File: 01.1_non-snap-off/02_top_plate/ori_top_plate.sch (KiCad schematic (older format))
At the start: 71 parts, among them U1 HOLE, U10 HOLE, U11 HOLE, U12 HOLE, U13 HOLE, U14 HOLE, U15 HOLE, U16 HOLE, U17 HOLE, U18 HOLE, U19 HOLE, U2 HOLE, U20 HOLE, U21 HOLE, U22 HOLE, U23 HOLE, U24 HOLE, U25 HOLE, U26 HOLE, U27 HOLE, U28 HOLE, U29 HOLE, U3 HOLE, U30 HOLE, U31 HOLE, U32 HOLE, U33 HOLE, U34 HOLE, U35 HOLE, U36 HOLE, U37 HOLE, U38 HOLE, U39 HOLE, U4 HOLE, U40 HOLE, U41 HOLE, U42 HOLE, U43 HOLE, U44 HOLE, U45 HOLE, U46 HOLE, U47 HOLE, U48 HOLE, U49 HOLE, U5 HOLE, U50 HOLE, U51 HOLE, U52 HOLE, U6 HOLE, U7 HOLE, U8 HOLE, U9 HOLE

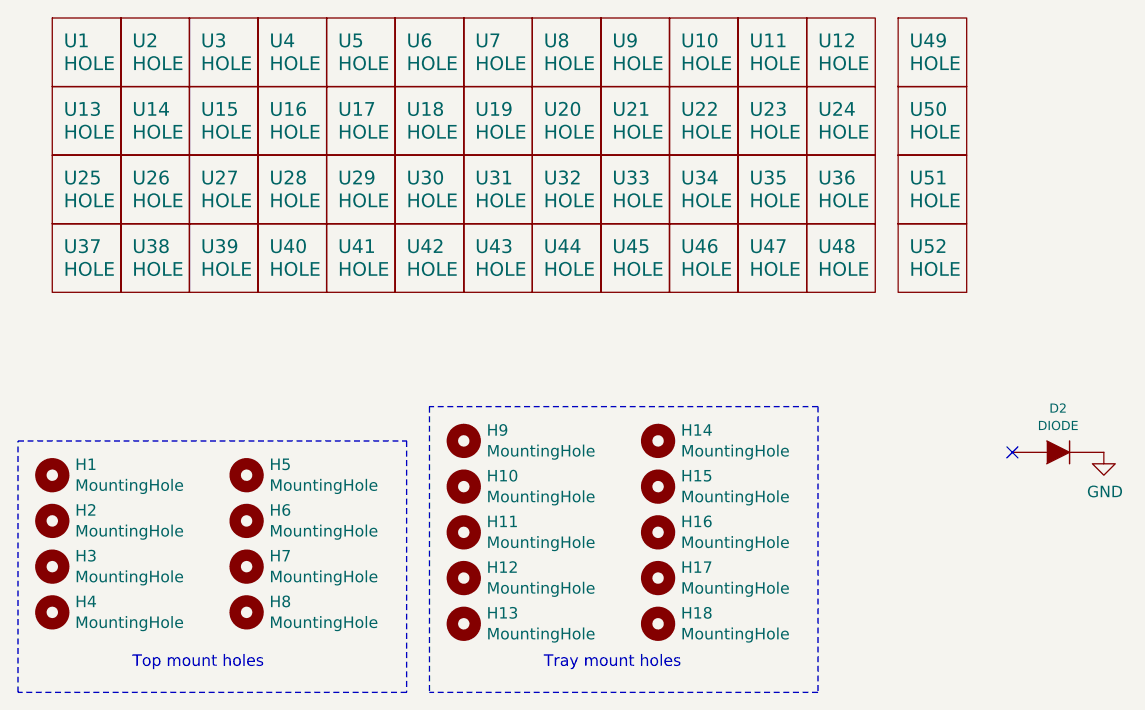
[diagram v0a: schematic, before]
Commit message: moved mounting holes
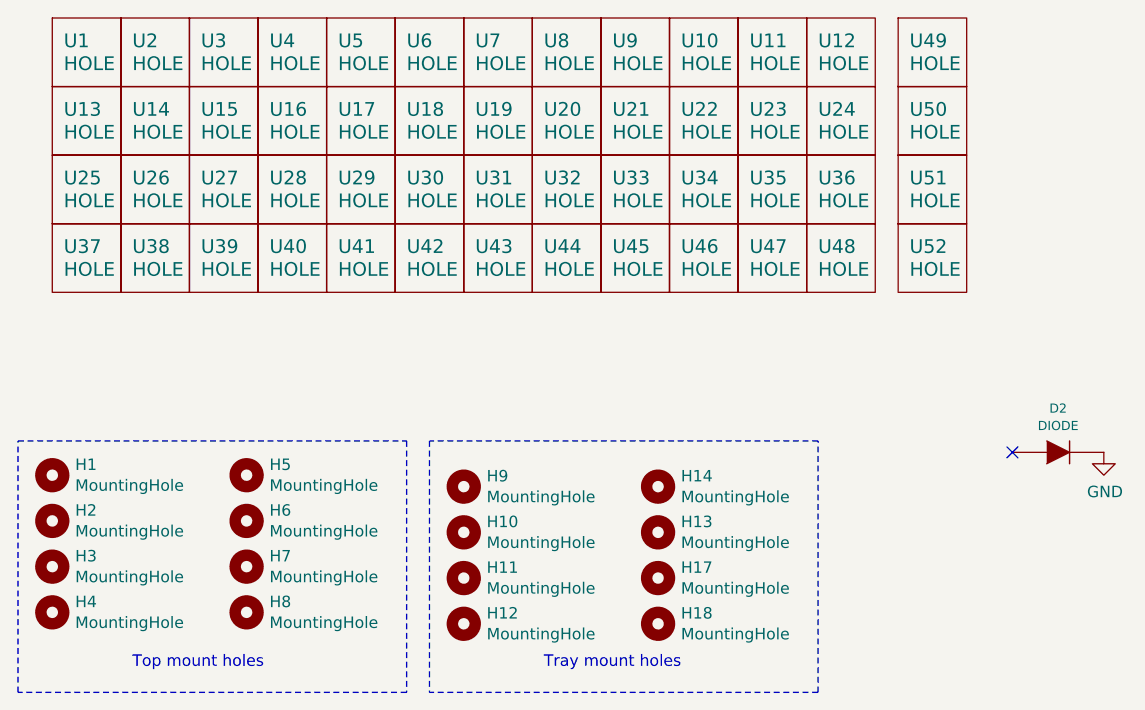
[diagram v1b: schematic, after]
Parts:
- removed H15, H16: MountingHole, MountingHole:MountingHole_2.2mm_M2_DIN965, symbol Mechanical:MountingHole
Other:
- moved on the sheet: H10, H11, H12, H13, H14, H9
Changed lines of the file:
@@
 L Mechanical:MountingHole H9
 U 1 1 6122943F
-P 4300 3250
-F 0 "H9" H 4400 3296 50  0000 L CNN
-F 1 "MountingHole" H 4400 3205 50  0000 L CNN
-F 2 "MountingHole:MountingHole_2.2mm_M2_DIN965" H 4300 3250 50  0001 C CNN
-F 3 "~" H 4300 3250 50  0001 C CNN
-	1    4300 3250
-	1    0    0    -1
-$EndComp
-$Comp
-L Mechanical:MountingHole H10
-U 1 1 61229445
 P 4300 3450
-F 0 "H10" H 4400 3496 50  0000 L CNN
+F 0 "H9" H 4400 3496 50  0000 L CNN
 F 1 "MountingHole" H 4400 3405 50  0000 L CNN
 F 2 "MountingHole:MountingHole_2.2mm_M2_DIN965" H 4300 3450 50  0001 C CNN
@@
 $EndComp
 $Comp
-L Mechanical:MountingHole H11
-U 1 1 6122944B
+L Mechanical:MountingHole H10
+U 1 1 61229445
 P 4300 3650
-F 0 "H11" H 4400 3696 50  0000 L CNN
+F 0 "H10" H 4400 3696 50  0000 L CNN
 F 1 "MountingHole" H 4400 3605 50  0000 L CNN
 F 2 "MountingHole:MountingHole_2.2mm_M2_DIN965" H 4300 3650 50  0001 C CNN
@@
 $EndComp
 $Comp
-L Mechanical:MountingHole H12
-U 1 1 61229451
+L Mechanical:MountingHole H11
+U 1 1 6122944B
 P 4300 3850
-F 0 "H12" H 4400 3896 50  0000 L CNN
+F 0 "H11" H 4400 3896 50  0000 L CNN
 F 1 "MountingHole" H 4400 3805 50  0000 L CNN
 F 2 "MountingHole:MountingHole_2.2mm_M2_DIN965" H 4300 3850 50  0001 C CNN
@@
 $EndComp
 $Comp
-L Mechanical:MountingHole H13
-U 1 1 61229457
+L Mechanical:MountingHole H12
+U 1 1 61229451
 P 4300 4050
-F 0 "H13" H 4400 4096 50  0000 L CNN
+F 0 "H12" H 4400 4096 50  0000 L CNN
 F 1 "MountingHole" H 4400 4005 50  0000 L CNN
 F 2 "MountingHole:MountingHole_2.2mm_M2_DIN965" H 4300 4050 50  0001 C CNN
@@
 $EndComp
 $Comp
-L Mechanical:MountingHole H14
-U 1 1 6122945D
-P 5150 3250
-F 0 "H14" H 5250 3296 50  0000 L CNN
-F 1 "MountingHole" H 5250 3205 50  0000 L CNN
-F 2 "MountingHole:MountingHole_2.2mm_M2_DIN965" H 5150 3250 50  0001 C CNN
-F 3 "~" H 5150 3250 50  0001 C CNN
-	1    5150 3250
+L Mechanical:MountingHole H13
+U 1 1 61229457
+P 5150 3650
+F 0 "H13" H 5250 3696 50  0000 L CNN
+F 1 "MountingHole" H 5250 3605 50  0000 L CNN
+F 2 "MountingHole:MountingHole_2.2mm_M2_DIN965" H 5150 3650 50  0001 C CNN
+F 3 "~" H 5150 3650 50  0001 C CNN
+	1    5150 3650
 	1    0    0    -1
 $EndComp
 $Comp
-L Mechanical:MountingHole H15
-U 1 1 61229463
+L Mechanical:MountingHole H14
+U 1 1 6122945D
 P 5150 3450
-F 0 "H15" H 5250 3496 50  0000 L CNN
+F 0 "H14" H 5250 3496 50  0000 L CNN
 F 1 "MountingHole" H 5250 3405 50  0000 L CNN
 F 2 "MountingHole:MountingHole_2.2mm_M2_DIN965" H 5150 3450 50  0001 C CNN
 F 3 "~" H 5150 3450 50  0001 C CNN
 	1    5150 3450
-	1    0    0    -1
-$EndComp
-$Comp
-L Mechanical:MountingHole H16
-U 1 1 61229469
-P 5150 3650
-F 0 "H16" H 5250 3696 50  0000 L CNN
-F 1 "MountingHole" H 5250 3605 50  0000 L CNN
-F 2 "MountingHole:MountingHole_2.2mm_M2_DIN965" H 5150 3650 50  0001 C CNN
-F 3 "~" H 5150 3650 50  0001 C CNN
-	1    5150 3650
 	1    0    0    -1
 $EndComp
@@
 $EndComp
 Wire Notes Line
-	5850 3100 4150 3100
+	5850 4350 5850 3250
 Wire Notes Line
-	5850 3100 5850 4350
+	5850 3250 4150 3250
 Wire Notes Line
-	4150 3100 4150 4350
+	4150 3250 4150 4350
 $EndSCHEMATC
